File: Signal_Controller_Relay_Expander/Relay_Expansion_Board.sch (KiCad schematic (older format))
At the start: 18 parts, among them J1 CONN_01X05, J2 CONN_01X02, J3 CONN_01X02, Q1 2N7002P,215, Q2 2N7002P,215, Q3 2N7002P,215

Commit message: Both boards mostly completed
just need final tweaks, silkscreen stuff etc, all major routing and
placement done
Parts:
- removed C1: 10uF, symbol C
- added C1: 100uF, Capacitors_THT:CP_Radial_D6.3mm_P2.50mm, symbol CP1
- D1: footprint (none) -> LEDs:LED_0603
- D2, D3, D4: value D_Schottky -> FM5819-W; footprint (none) -> Diodes_SMD:D_SMA_Standard
- J1: footprint (none) -> Pin_Headers:Pin_Header_Straight_1x05_Pitch2.54mm
- J2, J3: footprint (none) -> Connectors_Terminal_Blocks:TerminalBlock_Pheonix_PT-3.5mm_2pol
- Q1, Q2, Q3: footprint (none) -> TO_SOT_Packages_SMD:SOT-23
- R1, R2, R3, R4: footprint (none) -> Resistors_SMD:R_0603
- RL1, RL2, RL3: footprint (none) -> Global_Parts:G5LE-14-DC12
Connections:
- net +12V: now also C1.1
- net COIL_2A: now also J2.1 (P1); no longer J2.2 (P2)
- net COIL_2B: now also J2.2 (P2); no longer J2.1 (P1)
- net GND: now also C1.2
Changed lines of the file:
@@
 F 0 "RL1" H 7350 1850 50  0000 L CNN
 F 1 "G5LE-1" H 7350 1750 50  0000 L CNN
-F 2 "" H 6900 1700 50  0001 C CNN
+F 2 "Global_Parts:G5LE-14-DC12" H 6900 1700 50  0001 C CNN
 F 3 "" H 6900 1700 50  0001 C CNN
 	1    6900 1700
@@
 F 0 "RL2" H 7350 3750 50  0000 L CNN
 F 1 "G5LE-1" H 7350 3650 50  0000 L CNN
-F 2 "" H 6900 3600 50  0001 C CNN
+F 2 "Global_Parts:G5LE-14-DC12" H 6900 3600 50  0001 C CNN
 F 3 "" H 6900 3600 50  0001 C CNN
 	1    6900 3600
@@
 F 0 "RL3" H 7350 5650 50  0000 L CNN
 F 1 "G5LE-1" H 7350 5550 50  0000 L CNN
-F 2 "" H 6900 5500 50  0001 C CNN
+F 2 "Global_Parts:G5LE-14-DC12" H 6900 5500 50  0001 C CNN
 F 3 "" H 6900 5500 50  0001 C CNN
 	1    6900 5500
@@
 $EndComp
 $Comp
-L GND #PWR11
+L GND #PWR01
 U 1 1 58F816D3
 P 6500 6450
-F 0 "#PWR11" H 6500 6200 50  0001 C CNN
+F 0 "#PWR01" H 6500 6200 50  0001 C CNN
 F 1 "GND" H 6500 6300 50  0000 C CNN
 F 2 "" H 6500 6450 50  0001 C CNN
@@
 $EndComp
 $Comp
-L GND #PWR9
+L GND #PWR02
 U 1 1 58F816EE
 P 6500 2650
-F 0 "#PWR9" H 6500 2400 50  0001 C CNN
+F 0 "#PWR02" H 6500 2400 50  0001 C CNN
 F 1 "GND" H 6500 2500 50  0000 C CNN
 F 2 "" H 6500 2650 50  0001 C CNN
@@
 $EndComp
 $Comp
-L GND #PWR2
+L GND #PWR03
 U 1 1 58F81702
 P 4200 3150
-F 0 "#PWR2" H 4200 2900 50  0001 C CNN
+F 0 "#PWR03" H 4200 2900 50  0001 C CNN
 F 1 "GND" H 4200 3000 50  0000 C CNN
 F 2 "" H 4200 3150 50  0001 C CNN
@@
 F 0 "J1" H 4500 3150 50  0000 C CNN
 F 1 "CONN_01X05" V 4600 2850 50  0000 C CNN
-F 2 "" H 4500 2850 50  0001 C CNN
+F 2 "Pin_Headers:Pin_Header_Straight_1x05_Pitch2.54mm" H 4500 2850 50  0001 C CNN
 F 3 "" H 4500 2850 50  0001 C CNN
 	1    4500 2850
@@
 $EndComp
 $Comp
-L +12V #PWR1
+L +12V #PWR04
 U 1 1 58F81782
 P 4200 2550
-F 0 "#PWR1" H 4200 2400 50  0001 C CNN
+F 0 "#PWR04" H 4200 2400 50  0001 C CNN
 F 1 "+12V" H 4200 2690 50  0000 C CNN
 F 2 "" H 4200 2550 50  0001 C CNN
@@
 F 0 "Q2" H 7800 4150 50  0000 L CNN
 F 1 "2N7002P,215" H 7200 3900 50  0000 L CNN
-F 2 "" H 7800 4200 50  0001 C CNN
+F 2 "TO_SOT_Packages_SMD:SOT-23" H 7800 4200 50  0001 C CNN
 F 3 "" H 7600 4100 50  0001 C CNN
 	1    7600 4100
@@
 F 0 "Q3" H 7800 6050 50  0000 L CNN
 F 1 "2N7002P,215" H 7200 5800 50  0000 L CNN
-F 2 "" H 7800 6100 50  0001 C CNN
+F 2 "TO_SOT_Packages_SMD:SOT-23" H 7800 6100 50  0001 C CNN
 F 3 "" H 7600 6000 50  0001 C CNN
 	1    7600 6000
@@
 F 0 "Q1" H 7800 2250 50  0000 L CNN
 F 1 "2N7002P,215" H 7200 2000 50  0000 L CNN
-F 2 "" H 7800 2300 50  0001 C CNN
+F 2 "TO_SOT_Packages_SMD:SOT-23" H 7800 2300 50  0001 C CNN
 F 3 "" H 7600 2200 50  0001 C CNN
 	1    7600 2200
@@
 F 0 "R3" V 7930 4300 50  0000 C CNN
 F 1 "10K" V 7850 4300 50  0000 C CNN
-F 2 "" V 7780 4300 50  0001 C CNN
+F 2 "Resistors_SMD:R_0603" V 7780 4300 50  0001 C CNN
 F 3 "" H 7850 4300 50  0001 C CNN
 	1    7850 4300
@@
 F 0 "R2" V 7930 2400 50  0000 C CNN
 F 1 "10K" V 7850 2400 50  0000 C CNN
-F 2 "" V 7780 2400 50  0001 C CNN
+F 2 "Resistors_SMD:R_0603" V 7780 2400 50  0001 C CNN
 F 3 "" H 7850 2400 50  0001 C CNN
 	1    7850 2400
@@
 F 0 "R4" V 7930 6200 50  0000 C CNN
 F 1 "10K" V 7850 6200 50  0000 C CNN
-F 2 "" V 7780 6200 50  0001 C CNN
+F 2 "Resistors_SMD:R_0603" V 7780 6200 50  0001 C CNN
 F 3 "" H 7850 6200 50  0001 C CNN
 	1    7850 6200
@@
 F 0 "J3" H 4900 5000 50  0000 C CNN
 F 1 "CONN_01X02" V 5000 4850 50  0000 C CNN
-F 2 "" H 4900 4850 50  0001 C CNN
+F 2 "Connectors_Terminal_Blocks:TerminalBlock_Pheonix_PT-3.5mm_2pol" H 4900 4850 50  0001 C CNN
 F 3 "" H 4900 4850 50  0001 C CNN
 	1    4900 4850
@@
 F 0 "J2" H 4900 4300 50  0000 C CNN
 F 1 "CONN_01X02" V 5000 4150 50  0000 C CNN
-F 2 "" H 4900 4150 50  0001 C CNN
+F 2 "Connectors_Terminal_Blocks:TerminalBlock_Pheonix_PT-3.5mm_2pol" H 4900 4150 50  0001 C CNN
 F 3 "" H 4900 4150 50  0001 C CNN
 	1    4900 4150
 	1    0    0    1
 $EndComp
+Text HLabel 4600 4200 0    60   Input ~ 0
+COIL_2A
 Text HLabel 4600 4100 0    60   Input ~ 0
-COIL_2A
-Text HLabel 4600 4200 0    60   Input ~ 0
 COIL_2B
 Text HLabel 4600 4800 0    60   Input ~ 0
 BULB_2
 $Comp
-L GND #PWR3
+L GND #PWR05
 U 1 1 58F8274F
 P 4600 5000
-F 0 "#PWR3" H 4600 4750 50  0001 C CNN
+F 0 "#PWR05" H 4600 4750 50  0001 C CNN
 F 1 "GND" H 4600 4850 50  0000 C CNN
 F 2 "" H 4600 5000 50  0001 C CNN
@@
 Power and Signal Input
 $Comp
-L GND #PWR10
+L GND #PWR06
 U 1 1 58F84021
 P 6500 4550
-F 0 "#PWR10" H 6500 4300 50  0001 C CNN
+F 0 "#PWR06" H 6500 4300 50  0001 C CNN
 F 1 "GND" H 6500 4400 50  0000 C CNN
 F 2 "" H 6500 4550 50  0001 C CNN
@@
 P 6900 2350
 F 0 "D2" H 6900 2450 50  0000 C CNN
-F 1 "D_Schottky" H 6900 2250 50  0000 C CNN
-F 2 "" H 6900 2350 50  0001 C CNN
+F 1 "FM5819-W" H 6900 2250 50  0000 C CNN
+F 2 "Diodes_SMD:D_SMA_Standard" H 6900 2350 50  0001 C CNN
 F 3 "" H 6900 2350 50  0001 C CNN
 	1    6900 2350
@@
 	6500 1600 6600 1600
 $Comp
-L +12V #PWR6
+L +12V #PWR07
 U 1 1 58F85B4C
 P 6300 1250
-F 0 "#PWR6" H 6300 1100 50  0001 C CNN
+F 0 "#PWR07" H 6300 1100 50  0001 C CNN
 F 1 "+12V" H 6300 1390 50  0000 C CNN
 F 2 "" H 6300 1250 50  0001 C CNN
@@
 P 6900 4250
 F 0 "D3" H 6900 4350 50  0000 C CNN
-F 1 "D_Schottky" H 6900 4150 50  0000 C CNN
-F 2 "" H 6900 4250 50  0001 C CNN
+F 1 "FM5819-W" H 6900 4150 50  0000 C CNN
+F 2 "Diodes_SMD:D_SMA_Standard" H 6900 4250 50  0001 C CNN
 F 3 "" H 6900 4250 50  0001 C CNN
 	1    6900 4250
@@
 	6500 3500 6500 4550
 $Comp
-L +12V #PWR7
+L +12V #PWR08
 U 1 1 58F8678E
 P 6300 3150
-F 0 "#PWR7" H 6300 3000 50  0001 C CNN
+F 0 "#PWR08" H 6300 3000 50  0001 C CNN
 F 1 "+12V" H 6300 3290 50  0000 C CNN
 F 2 "" H 6300 3150 50  0001 C CNN
@@
 	6300 5700 6600 5700
 $Comp
-L +12V #PWR8
+L +12V #PWR09
 U 1 1 58F87437
 P 6300 5050
-F 0 "#PWR8" H 6300 4900 50  0001 C CNN
+F 0 "#PWR09" H 6300 4900 50  0001 C CNN
 F 1 "+12V" H 6300 5190 50  0000 C CNN
 F 2 "" H 6300 5050 50  0001 C CNN
@@
 P 6900 6150
 F 0 "D4" H 6900 6250 50  0000 C CNN
-F 1 "D_Schottky" H 6900 6050 50  0000 C CNN
-F 2 "" H 6900 6150 50  0001 C CNN
+F 1 "FM5819-W" H 6900 6050 50  0000 C CNN
+F 2 "Diodes_SMD:D_SMA_Standard" H 6900 6150 50  0001 C CNN
 F 3 "" H 6900 6150 50  0001 C CNN
 	1    6900 6150
@@
 	7400 1500 7200 1500
 $Comp
-L +12V #PWR4
+L +12V #PWR010
 U 1 1 58F891D2
 P 4850 2400
-F 0 "#PWR4" H 4850 2250 50  0001 C CNN
+F 0 "#PWR010" H 4850 2250 50  0001 C CNN
 F 1 "+12V" H 4850 2540 50  0000 C CNN
 F 2 "" H 4850 2400 50  0001 C CNN
@@
 F 0 "R1" V 4930 2650 50  0000 C CNN
 F 1 "R" V 4850 2650 50  0000 C CNN
-F 2 "" V 4780 2650 50  0001 C CNN
+F 2 "Resistors_SMD:R_0603" V 4780 2650 50  0001 C CNN
 F 3 "" H 4850 2650 50  0001 C CNN
 	1    4850 2650
@@
 F 0 "D1" H 4850 3150 50  0000 C CNN
 F 1 "LED" H 4850 2950 50  0000 C CNN
-F 2 "" H 4850 3050 50  0001 C CNN
+F 2 "LEDs:LED_0603" H 4850 3050 50  0001 C CNN
 F 3 "" H 4850 3050 50  0001 C CNN
 	1    4850 3050
@@
 $EndComp
 $Comp
-L GND #PWR5
+L GND #PWR011
 U 1 1 58F892BE
 P 4850 3300
-F 0 "#PWR5" H 4850 3050 50  0001 C CNN
+F 0 "#PWR011" H 4850 3050 50  0001 C CNN
 F 1 "GND" H 4850 3150 50  0000 C CNN
 F 2 "" H 4850 3300 50  0001 C CNN
@@
 	1    0    0    -1
 $EndComp
-$Comp
-L C C1
-U 1 1 58F892ED
+Wire Wire Line
+	5100 2700 5100 2450
+Wire Wire Line
+	5100 2450 4850 2450
+Wire Wire Line
+	4850 2400 4850 2500
+Connection ~ 4850 2450
+Wire Wire Line
+	5100 3000 5100 3250
+Wire Wire Line
+	5100 3250 4850 3250
+Wire Wire Line
+	4850 3200 4850 3300
+Connection ~ 4850 3250
+Wire Wire Line
+	4850 2900 4850 2800
+$Comp
+L CP1 C1
+U 1 1 58FAB065
 P 5100 2850
 F 0 "C1" H 5125 2950 50  0000 L CNN
-F 1 "10uF" H 5125 2750 50  0000 L CNN
-F 2 "" H 5138 2700 50  0001 C CNN
+F 1 "100uF" H 5125 2750 50  0000 L CNN
+F 2 "Capacitors_THT:CP_Radial_D6.3mm_P2.50mm" H 5100 2850 50  0001 C CNN
 F 3 "" H 5100 2850 50  0001 C CNN
 	1    5100 2850
 	1    0    0    -1
 $EndComp
-Wire Wire Line
-	5100 2700 5100 2450
-Wire Wire Line
-	5100 2450 4850 2450
-Wire Wire Line
-	4850 2400 4850 2500
-Connection ~ 4850 2450
-Wire Wire Line
-	5100 3000 5100 3250
-Wire Wire Line
-	5100 3250 4850 3250
-Wire Wire Line
-	4850 3200 4850 3300
-Connection ~ 4850 3250
-Wire Wire Line
-	4850 2900 4850 2800
 $EndSCHEMATC

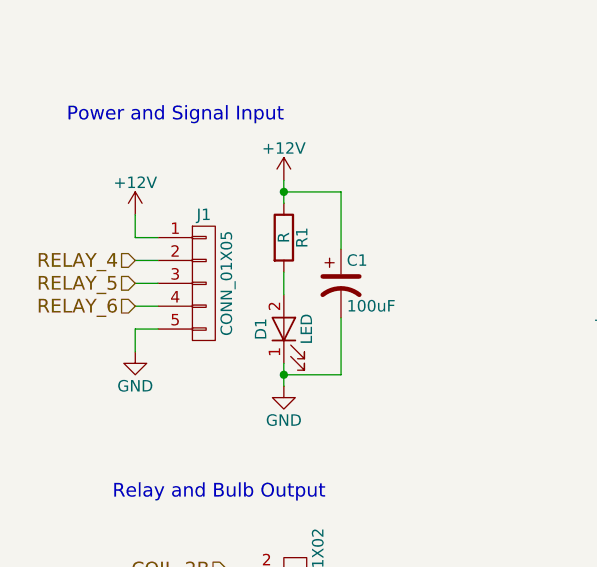
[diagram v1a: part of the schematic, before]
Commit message: moved relays and connector to line up with controller board
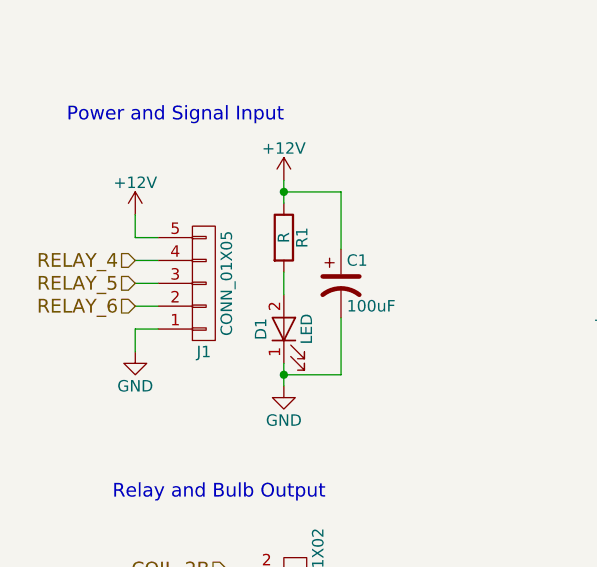
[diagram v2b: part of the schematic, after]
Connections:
- net +12V: now also J1.5 (P5); no longer J1.1 (P1)
- net GND: now also J1.1 (P1); no longer J1.5 (P5)
- net RELAY_4: now also J1.4 (P4); no longer J1.2 (P2)
- net RELAY_6: now also J1.2 (P2); no longer J1.4 (P4)
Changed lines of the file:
@@
 LIBS:contrib
 LIBS:valves
-LIBS:Global_Parts
 LIBS:Relay_Expansion_Board-cache
 EELAYER 25 0
@@
 F 3 "" H 4500 2850 50  0001 C CNN
 	1    4500 2850
-	1    0    0    -1
+	1    0    0    1
 $EndComp
 $Comp
